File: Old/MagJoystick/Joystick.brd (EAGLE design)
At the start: 30.5 x 33 mm, 10 parts, among them SW1 TopUp EC12PLRGBSDVBF-D, U1 attiny841-ssur

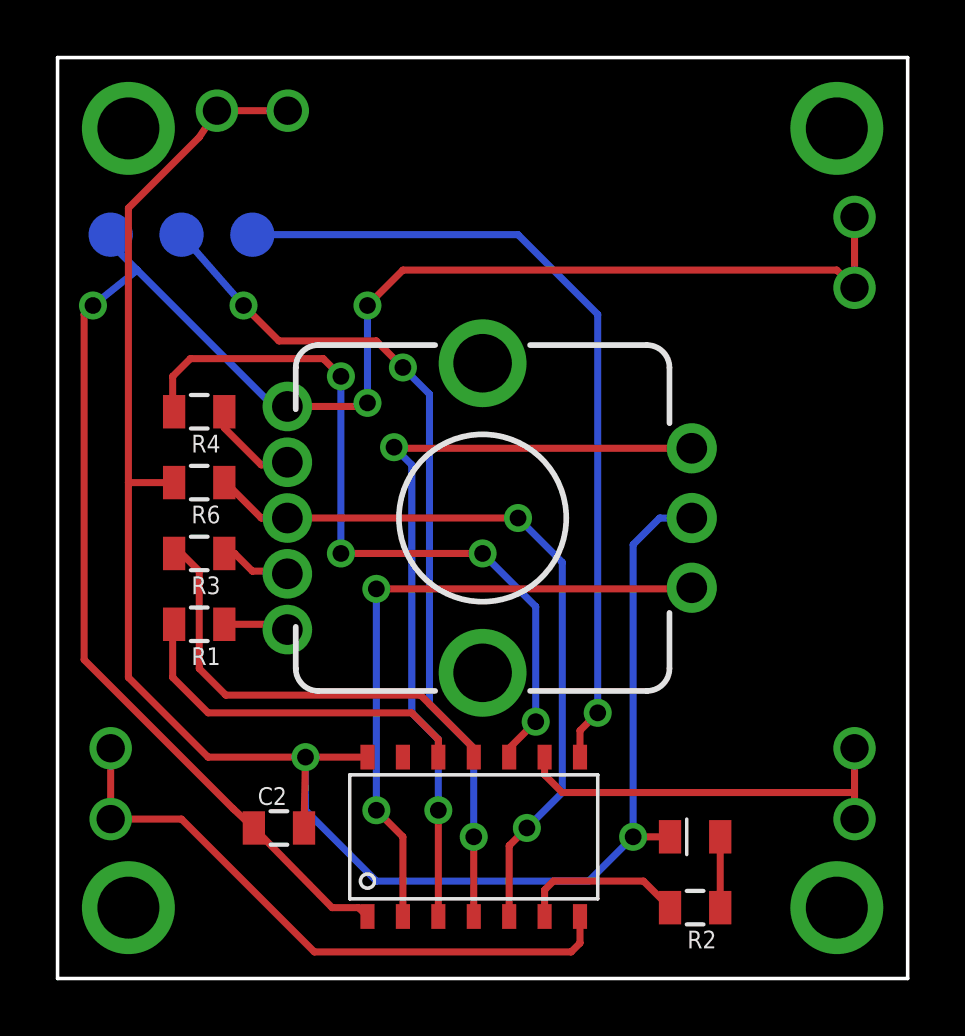
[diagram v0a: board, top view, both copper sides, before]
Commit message: Moved a bunch of files around
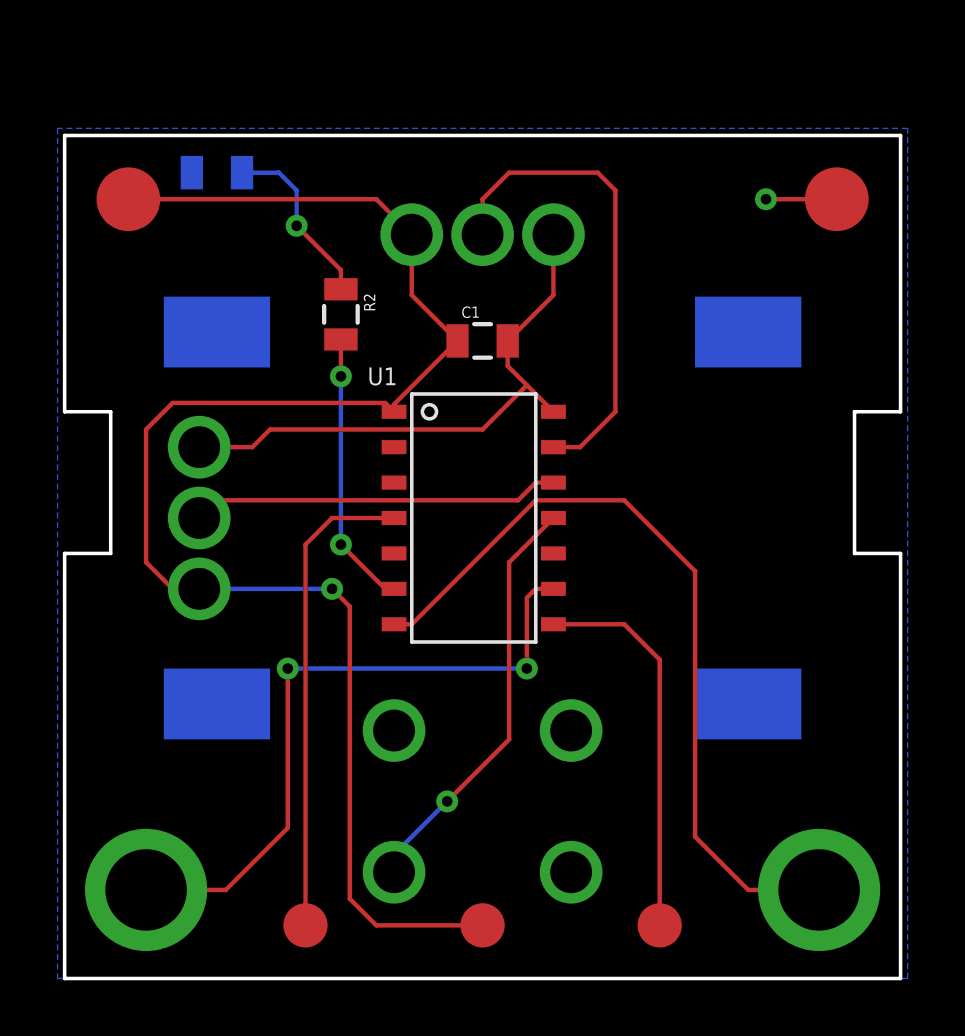
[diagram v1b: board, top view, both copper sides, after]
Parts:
- removed C2: .47uF, Modulo:0805
- removed R1: 130, Modulo:0805
- removed R3, R4: 68, Modulo:0805
- removed R6: 2k, Modulo:0805
- removed SW1: TopUp EC12PLRGBSDVBF-D, SparkFun-Electromechanical:ENCODER_LED_3
- added C1: .47uF, SparkFun-Capacitors:0805
- added J1: JOYSTICKPTH, Modulo:JOYSTICK
- LED1: value LTST-C171TBKT -> blue
- PCB1: value MAGDEVICE -> MAGDEVICE-V2; device Modulo:MAGDEVICE -> Modulo:MAGDEVICE-V2
- R2: device Modulo:0805 -> SparkFun-Passives:0805
- U1: value attiny841-ssur -> ATTINY841-SSUR; device IntegerLabs:SOIC14 -> Modulo:SOIC-14
- moved PCB1 30.5 mm to (30.5, 0.00), flipped to the bottom
- moved LED1 29.3 mm to (5.71, 28.9), flipped to the bottom, turned to 270 degrees
- moved R2 24.8 mm to (10.2, 23.8), turned to 270 degrees
- moved U1 15.5 mm to (15.2, 20.3), turned to 270 degrees
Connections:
- net MISO renamed N$2
- net RESET renamed N$3
- removed net A: SW1.A, U1.2
- removed net B: SW1.B, U1.3
- removed net BLUE: R4.2, U1.10
- removed net GREEN: R3.2, U1.11
- removed net N$6: R4.1, SW1.4
- removed net RED: R1.2, U1.12
- removed net SCL/SCK: PCB1.SCLA, PCB1.SCLB, U1.9
- removed net SDA/MOSI: PCB1.SDAA, PCB1.SDAB, U1.7
- removed net SW: R6.1, SW1.3, U1.5
- new net H: J1.H2, U1.13
- new net SEL: J1.B1A, U1.11
- new net V: J1.V2, U1.12
- net GND: now also C1.2, J1.B2A, J1.H3, J1.V3, PCB1.GND; no longer C2.2, PCB1.GNDA, PCB1.GNDB, R6.2, SW1.C
- net N$4: now also PCB1.SCL, U1.9; no longer R1.1, SW1.1
- net N$5: now also PCB1.SDA, U1.7; no longer R3.1, SW1.2
- net VCC: now also C1.1, J1.H1, J1.V1, PCB1.VCC; no longer C2.1, PCB1.VCCA, PCB1.VCCB, SW1.5
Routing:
- net GND: track 67.7 -> 22.9 mm, vias 2 -> 1
- net B: track 28.2 -> 0.00 mm, vias 2 -> 0
- net BLUE: track 27.8 -> 0.00 mm, vias 4 -> 0
- net SW: track 26.8 -> 0.00 mm, vias 2 -> 0
- net N$5: track 2.54 -> 28.4 mm
- net A: track 23.5 -> 0.00 mm, vias 2 -> 0
- net SDA/MOSI: track 22.4 -> 0.00 mm
- net N$4: track 2.34 -> 23.9 mm, vias 0 -> 2
- net H: track 0.00 -> 17.4 mm
- net GREEN: track 16.0 -> 0.00 mm
- net N$2: track 29.7 -> 13.9 mm, vias 1 -> 0
- net SEL: track 0.00 -> 15.1 mm, vias 0 -> 1
- net SCL/SCK: track 14.6 -> 0.00 mm
- net N$3: track 30.7 -> 17.2 mm, vias 3 -> 0
- net V: track 0.00 -> 13.2 mm
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- added copper zone on layer 16, net GND
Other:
- board size 30.5 x 33 mm -> 30 x 30.2 mm
